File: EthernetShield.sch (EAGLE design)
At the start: 74 parts, among them IC1 W5100SQFP80, IC2 MCP24AA025E48, Q1 2N7002, SW1 RESET

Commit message: Updates for release v2.0
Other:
- note added: "SKU: ES"
- note added: "www.freetronics.org/es"
- note removed: "SH-ETHERNET"
- note removed: "www.freetronics.org"
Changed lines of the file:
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@@
 <text x="7.62" y="12.7" size="3.048" layer="94">Freetronics Ethernet Shield for Arduino</text>
 <text x="81.28" y="6.858" size="1.778" layer="94">V2.0 (3-Jul-2013)</text>
-<text x="7.366" y="6.858" size="1.778" layer="94">www.freetronics.org</text>
-<text x="40.64" y="6.858" size="1.778" layer="94">SH-ETHERNET</text>
+<text x="7.366" y="6.858" size="1.778" layer="94">www.freetronics.org/es</text>
+<text x="48.26" y="6.858" size="1.778" layer="94">SKU: ES</text>
 <text x="33.02" y="177.8" size="1.778" layer="94">3V3 Power Supply</text>
 <text x="195.58" y="177.8" size="1.778" layer="94">Status Display</text>
@@
 <frame x1="0" y1="0" x2="248.92" y2="185.42" columns="8" rows="5" layer="94"/>
 <frame x1="5.08" y1="5.08" x2="109.22" y2="17.78" columns="0" rows="0" layer="94" border-left="no" border-top="no" border-right="no" border-bottom="no"/>
-<frame x1="38.1" y1="5.08" x2="78.74" y2="10.16" columns="8" rows="5" layer="94"/>
+<frame x1="45.72" y1="5.08" x2="78.74" y2="10.16" columns="8" rows="5" layer="94"/>
 <frame x1="78.74" y1="5.08" x2="109.22" y2="10.16" columns="8" rows="5" layer="94"/>
 <frame x1="0" y1="190.5" x2="248.92" y2="375.92" columns="8" rows="5" layer="94"/>

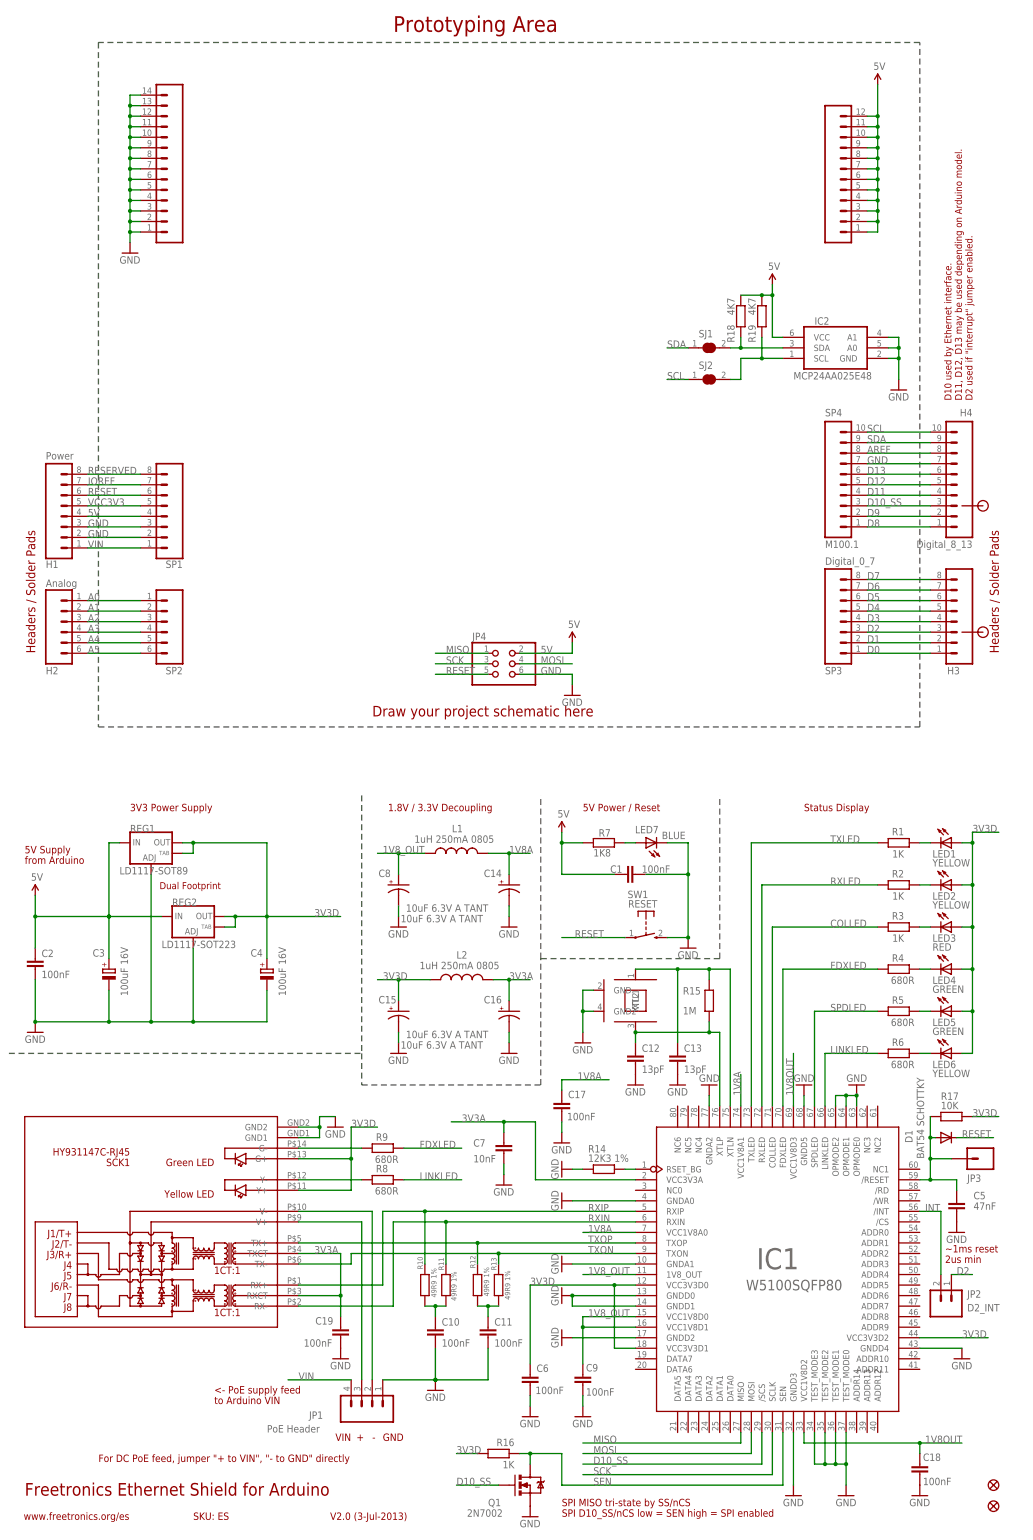
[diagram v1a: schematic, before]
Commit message: Changed I2C pull-ups to use IOREF, and added isolation jumpers
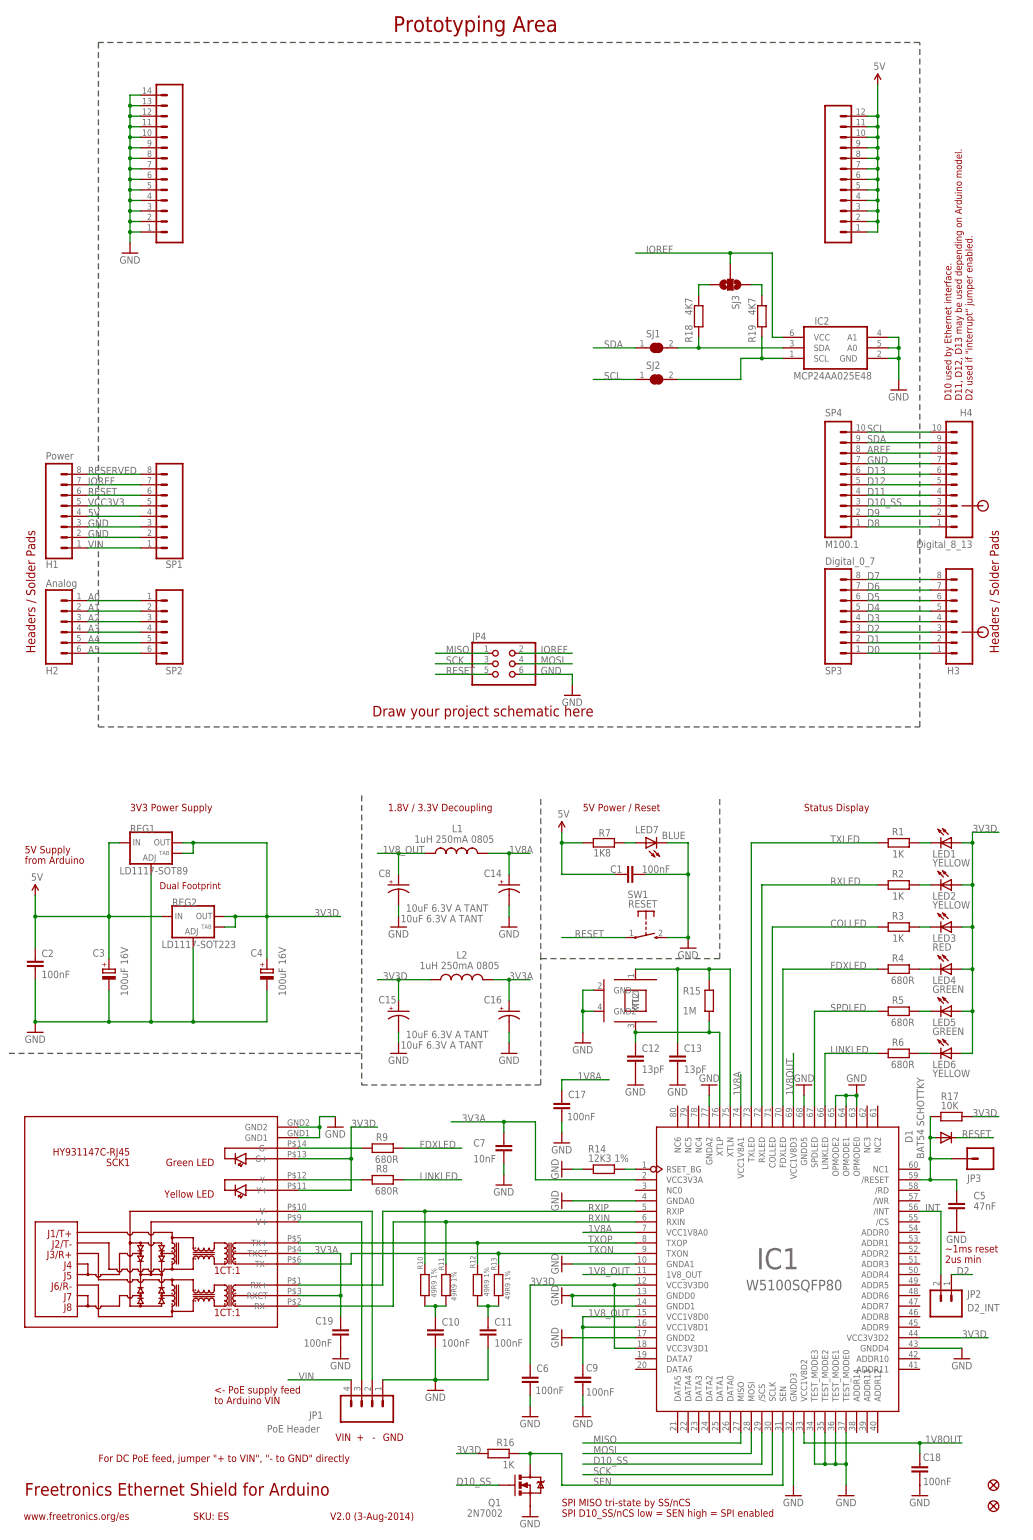
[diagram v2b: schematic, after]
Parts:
- added SJ3: (no value), freetronics-original:SOLDERJUMPER_2WAYT
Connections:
- new net N$53: R19.1, SJ3.1
- new net N$7: R18.1, SJ3.3
- net 5V: no longer IC2.VCC, JP4.2, R18.1, R19.1
- net IOREF: now also IC2.VCC, JP4.2, SJ3.2
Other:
- note added: "V2.0 (3-Aug-2014)"
- note removed: "V2.0 (3-Jul-2013)"
- moved on the sheet: R18, SJ1, SJ2
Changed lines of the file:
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@@
 <?xml version="1.0" encoding="utf-8"?>
 <!DOCTYPE eagle SYSTEM "eagle.dtd">
-<eagle version="6.3">
+<eagle version="6.5.0">
 <drawing>
 <settings>
@@
 <part name="JP4" library="freetronics-master-v1.1" deviceset="PINHD-2X3" device=""/>
 <part name="GND31" library="freetronics" deviceset="GND" device=""/>
-<part name="U$1" library="SparkFun" deviceset="5V" device=""/>
 <part name="XTL1" library="freetronics-jon" deviceset="CRYSTAL-GND" device="3X2" value="25MHZ"/>
 <part name="GND32" library="freetronics" deviceset="GND" device=""/>
 <part name="SW1" library="freetronics-master-v1" deviceset="TAC_SWITCH_2PIN" device="" value="RESET"/>
 <part name="IC2" library="freetronics-jon" deviceset="MCP24AA025E48" device=""/>
-<part name="U$9" library="SparkFun" deviceset="5V" device=""/>
 <part name="GND42" library="freetronics" deviceset="GND" device=""/>
 <part name="R18" library="freetronics-master-v1.1" deviceset="RESISTOR" device="0603" value="4K7"/>
@@
 <part name="SJ1" library="freetronics-jon" deviceset="SJC" device="N" value=""/>
 <part name="SJ2" library="freetronics-jon" deviceset="SJC" device="N" value=""/>
+<part name="SJ3" library="freetronics-original" deviceset="SOLDERJUMPER_2WAY" device="T"/>
 </parts>
 <sheets>
@@
 <text x="96.52" y="365.76" size="3.81" layer="94" ratio="12">Prototyping Area</text>
 <text x="7.62" y="12.7" size="3.048" layer="94">Freetronics Ethernet Shield for Arduino</text>
-<text x="81.28" y="6.858" size="1.778" layer="94">V2.0 (3-Jul-2013)</text>
+<text x="81.28" y="6.858" size="1.778" layer="94">V2.0 (3-Aug-2014)</text>
 <text x="7.366" y="6.858" size="1.778" layer="94">www.freetronics.org/es</text>
 <text x="48.26" y="6.858" size="1.778" layer="94">SKU: ES</text>
@@
 <instance part="JP4" gate="A" x="121.92" y="213.36"/>
 <instance part="GND31" gate="1" x="139.7" y="205.74"/>
-<instance part="U$1" gate="G$1" x="139.7" y="218.44"/>
 <instance part="XTL1" gate="G$1" x="154.94" y="132.08" rot="R270"/>
 <instance part="GND32" gate="1" x="142.24" y="121.92"/>
@@
 <attribute name="VALUE" x="193.04" y="281.94" size="1.778" layer="95"/>
 </instance>
-<instance part="U$9" gate="G$1" x="187.96" y="304.8"/>
 <instance part="GND42" gate="1" x="218.44" y="279.4"/>
-<instance part="R18" gate="G$1" x="180.34" y="297.18" smashed="yes" rot="R270">
-<attribute name="NAME" x="178.8414" y="290.83" size="1.778" layer="95" rot="R90"/>
-<attribute name="VALUE" x="178.8414" y="297.434" size="1.778" layer="96" rot="R90"/>
+<instance part="R18" gate="G$1" x="170.18" y="297.18" smashed="yes" rot="R270">
+<attribute name="NAME" x="168.6814" y="290.83" size="1.778" layer="95" rot="R90"/>
+<attribute name="VALUE" x="168.6814" y="297.434" size="1.778" layer="96" rot="R90"/>
 </instance>
 <instance part="R19" gate="G$1" x="185.42" y="297.18" smashed="yes" rot="R270">
@@
 <attribute name="VALUE" x="183.9214" y="297.434" size="1.778" layer="96" rot="R90"/>
 </instance>
-<instance part="SJ1" gate="G$1" x="172.72" y="289.56"/>
-<instance part="SJ2" gate="G$1" x="172.72" y="281.94"/>
+<instance part="SJ1" gate="G$1" x="160.02" y="289.56"/>
+<instance part="SJ2" gate="G$1" x="160.02" y="281.94"/>
+<instance part="SJ3" gate="G$1" x="177.8" y="304.8" rot="R270"/>
 </instances>
 <busses>
@@
 <pinref part="C1" gate="G$1" pin="1"/>
 </segment>
-<segment>
-<pinref part="JP4" gate="A" pin="2"/>
-<wire x1="127" y1="215.9" x2="139.7" y2="215.9" width="0.1524" layer="91"/>
-<label x="132.08" y="215.9" size="1.778" layer="95"/>
-<pinref part="U$1" gate="G$1" pin="5V"/>
-<wire x1="139.7" y1="215.9" x2="139.7" y2="218.44" width="0.1524" layer="91"/>
-</segment>
-<segment>
-<pinref part="IC2" gate="G$1" pin="VCC"/>
-<wire x1="190.5" y1="292.1" x2="187.96" y2="292.1" width="0.1524" layer="91"/>
-<wire x1="187.96" y1="292.1" x2="187.96" y2="302.26" width="0.1524" layer="91"/>
-<pinref part="U$9" gate="G$1" pin="5V"/>
-<pinref part="R18" gate="G$1" pin="1"/>
-<pinref part="R19" gate="G$1" pin="1"/>
-<wire x1="187.96" y1="302.26" x2="187.96" y2="304.8" width="0.1524" layer="91"/>
-<wire x1="180.34" y1="302.26" x2="185.42" y2="302.26" width="0.1524" layer="91"/>
-<wire x1="185.42" y1="302.26" x2="187.96" y2="302.26" width="0.1524" layer="91"/>
-<junction x="185.42" y="302.26"/>
-<junction x="187.96" y="302.26"/>
-</segment>
 </net>
 <net name="1V8_OUT" class="0">
@@
 <label x="22.86" y="256.54" size="1.778" layer="95"/>
 </segment>
+<segment>
+<pinref part="IC2" gate="G$1" pin="VCC"/>
+<wire x1="190.5" y1="292.1" x2="187.96" y2="292.1" width="0.1524" layer="91"/>
+<pinref part="SJ3" gate="G$1" pin="2"/>
+<wire x1="177.8" y1="309.88" x2="177.8" y2="312.42" width="0.1524" layer="91"/>
+<wire x1="177.8" y1="312.42" x2="187.96" y2="312.42" width="0.1524" layer="91"/>
+<wire x1="187.96" y1="312.42" x2="187.96" y2="292.1" width="0.1524" layer="91"/>
+<wire x1="177.8" y1="312.42" x2="154.94" y2="312.42" width="0.1524" layer="91"/>
+<junction x="177.8" y="312.42"/>
+<label x="157.48" y="312.42" size="1.778" layer="95"/>
+</segment>
+<segment>
+<pinref part="JP4" gate="A" pin="2"/>
+<wire x1="127" y1="215.9" x2="139.7" y2="215.9" width="0.1524" layer="91"/>
+<label x="132.08" y="215.9" size="1.778" layer="95"/>
+</segment>
 </net>
 <net name="RESERVED" class="0">
@@
 <segment>
 <pinref part="SJ1" gate="G$1" pin="1"/>
-<wire x1="167.64" y1="289.56" x2="162.56" y2="289.56" width="0.1524" layer="91"/>
-<label x="162.56" y="289.56" size="1.778" layer="95"/>
+<wire x1="154.94" y1="289.56" x2="144.78" y2="289.56" width="0.1524" layer="91"/>
+<label x="147.32" y="289.56" size="1.778" layer="95"/>
 </segment>
 </net>
@@
 <segment>
 <pinref part="SJ2" gate="G$1" pin="1"/>
-<wire x1="167.64" y1="281.94" x2="162.56" y2="281.94" width="0.1524" layer="91"/>
-<label x="162.56" y="281.94" size="1.778" layer="95"/>
+<wire x1="154.94" y1="281.94" x2="144.78" y2="281.94" width="0.1524" layer="91"/>
+<label x="147.32" y="281.94" size="1.778" layer="95"/>
 </segment>
 </net>
@@
 <wire x1="180.34" y1="287.02" x2="180.34" y2="281.94" width="0.1524" layer="91"/>
 <pinref part="SJ2" gate="G$1" pin="2"/>
-<wire x1="180.34" y1="281.94" x2="177.8" y2="281.94" width="0.1524" layer="91"/>
+<wire x1="180.34" y1="281.94" x2="165.1" y2="281.94" width="0.1524" layer="91"/>
 <pinref part="R19" gate="G$1" pin="2"/>
 <wire x1="185.42" y1="292.1" x2="185.42" y2="287.02" width="0.1524" layer="91"/>
@@
 <segment>
 <pinref part="IC2" gate="G$1" pin="SDA"/>
-<wire x1="190.5" y1="289.56" x2="180.34" y2="289.56" width="0.1524" layer="91"/>
+<wire x1="190.5" y1="289.56" x2="170.18" y2="289.56" width="0.1524" layer="91"/>
 <pinref part="SJ1" gate="G$1" pin="2"/>
 <pinref part="R18" gate="G$1" pin="2"/>
-<wire x1="180.34" y1="289.56" x2="177.8" y2="289.56" width="0.1524" layer="91"/>
-<wire x1="180.34" y1="292.1" x2="180.34" y2="289.56" width="0.1524" layer="91"/>
-<junction x="180.34" y="289.56"/>
-</segment>
-</net>
+<wire x1="170.18" y1="289.56" x2="165.1" y2="289.56" width="0.1524" layer="91"/>
+<wire x1="170.18" y1="292.1" x2="170.18" y2="289.56" width="0.1524" layer="91"/>
+<junction x="170.18" y="289.56"/>
+</segment>
+</net>
+<net name="N$7" class="0">
+<segment>
+<pinref part="R18" gate="G$1" pin="1"/>
+<wire x1="170.18" y1="302.26" x2="170.18" y2="304.8" width="0.1524" layer="91"/>
+<pinref part="SJ3" gate="G$1" pin="3"/>
+<wire x1="170.18" y1="304.8" x2="172.72" y2="304.8" width="0.1524" layer="91"/>
+</segment>
+</net>
+<net name="N$53" class="0">
+<segment>
+<pinref part="R19" gate="G$1" pin="1"/>
+<wire x1="185.42" y1="302.26" x2="185.42" y2="304.8" width="0.1524" layer="91"/>
+<pinref part="SJ3" gate="G$1" pin="1"/>
+<wire x1="185.42" y1="304.8" x2="182.88" y2="304.8" width="0.1524" layer="91"/>
+</segment>
+</net>

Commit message: Added info about I2C address
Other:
- note added: "MCP24AA025E I2C ADDR: 0x50"
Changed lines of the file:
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@@
 <text x="53.34" y="34.798" size="1.778" layer="94">to Arduino VIN</text>
 <text x="233.68" y="276.86" size="1.6764" layer="94" ratio="12" rot="R90">D11, D12, D13 may be used depending on Arduino model.</text>
+<text x="172.72" y="274.32" size="1.9304" layer="94" ratio="10">MCP24AA025E I2C
+ADDR: 0x50</text>
 </plain>
 <instances>
@@
 </schematic>
 </drawing>
+<compatibility>
+<note version="6.3" minversion="6.2.2" severity="warning">
+Since Version 6.2.2 text objects can contain more than one line,
+which will not be processed correctly with this version.
+</note>
+</compatibility>
 </eagle>
